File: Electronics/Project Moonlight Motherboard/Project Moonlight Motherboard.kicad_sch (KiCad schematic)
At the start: 42 parts, among them M1 AO3400A, M2 AO3400A, M3 AO3400A, U1 STM32F407IEHx, U2 TMC2209_SILENTSTEPSTICK, U3 TMC2209_SILENTSTEPSTICK, U4 TMC2209_SILENTSTEPSTICK, U5 TMC2209_SILENTSTEPSTICK

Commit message: whoops forgor to save it
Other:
- note added: "Auto Bed Leveling"
- note added: "Bed and Heater Mosfets"
- note added: "Fan Mosfets"
- note added: "I2C Display and Encoder"
- note added: "Power LED"
- note added: "Removable Stepper Drivers (XYZE)"
- note added: "Thermistors (T0, T1, T2)"
- moved on the sheet: ABL1, BED1, C1, C2, C3, C4, C5, C6, C7, FAN1, FAN2, FAN3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

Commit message: added a fuse
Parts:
- added F1: Fuse_Small, symbol Device:Fuse_Small
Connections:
- net VCC: now also F1.2; no longer PWR_IN.02
- new net: F1.1, PWR_IN.02
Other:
- moved on the sheet: PWR_IN

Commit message: fixed schematic & added 3d model for MCU
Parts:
- removed PWR_IN: 1751248, Phoenix 1751248:PHOENIX_1751248, symbol 1751248:1751248
- renumbered Z_END to Z_END1
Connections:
- net VCC: no longer PWR1.1
- net at F1.1: now also PWR1.1
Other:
- note added: "Power Jack"
- note removed: "Power LED"
- moved on the sheet: PWR1

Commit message: slowly updating lmao
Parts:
- added U6: STM32H563VITx, Package_QFP:LQFP-100_14x14mm_P0.5mm, symbol MCU_ST_STM32H5:STM32H563VITx
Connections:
- net +3V3: now also U6.100 (VDD), U6.11 (VDD), U6.22 (VDDA), U6.28 (VDD), U6.50 (VDD), U6.6 (VBAT), U6.73 (VDDUSB), U6.75 (VDD); no longer U1.C1 (VBAT), U1.C5 (VDD), U1.C7 (VDD), U1.C8 (VDD), U1.C9 (VDD), U1.F3 (VDD), U1.G13 (VDD), U1.G3 (VDD), U1.H13 (VDD), U1.J12 (VDD), U1.J13 (VDD), U1.K4 (VDD), U1.N10 (VDD), U1.N8 (VDD), U1.N9 (VDD), U1.R1 (VDDA)
- net ABL: now also U6.69 (PA10); no longer U1.D15 (PA10)
- net BED: now also U6.30 (PA5); no longer U1.P4 (PA5)
- net DIAG_M1: now also U6.18 (PC3); no longer U1.A10 (PB3)
- net DIAG_M2: now also U6.64 (PC7); no longer U1.B5 (PB7)
- net DIAG_M3: now also U6.79 (PC11); no longer U1.R13 (PB11)
- net DIAG_M4: now also U6.9 (PC15); no longer U1.R15 (PB15)
- net DIR_M1: now also U6.17 (PC2); no longer U1.M6 (PB2)
- net DIR_M2: now also U6.63 (PC6); no longer U1.B6 (PB6)
- net DIR_M3: now also U6.78 (PC10); no longer U1.R12 (PB10)
- net DIR_M4: now also U6.8 (PC14); no longer U1.R14 (PB14)
- net EN_BTN: now also U6.85 (PD4); no longer U1.J3 (PF4)
- net EN_FOR: now also U6.83 (PD2); no longer U1.H2 (PF2)
- net EN_M1: now also U6.15 (PC0); no longer U1.R5 (PB0)
- net EN_M2: now also U6.33 (PC4); no longer U1.A9 (PB4)
- net EN_M3: now also U6.65 (PC8); no longer U1.A5 (PB8)
- net EN_M4: now also U6.80 (PC12); no longer U1.P12 (PB12)
- net EN_REV: now also U6.84 (PD3); no longer U1.J2 (PF3)
- net FAN1: now also U6.31 (PA6); no longer U1.P3 (PA6)
- net FAN2: now also U6.32 (PA7); no longer U1.R3 (PA7)
- net FAN3: now also U6.67 (PA8); no longer U1.F15 (PA8)
- net GNDREF: now also U6.10 (VSS), U6.19 (VSSA), U6.27 (VSS), U6.49 (VSS), U6.74 (VSS), U6.99 (VSS); no longer U1.D5 (VSS), U1.D7 (VSS), U1.D8 (VSS), U1.D9 (VSS), U1.F10 (VSS), U1.F12 (VSS), U1.F2 (VSS), U1.F6 (VSS), U1.F7 (VSS), U1.F8 (VSS), U1.F9 (VSS), U1.G10 (VSS), U1.G12 (VSS), U1.G2 (VSS), U1.G6 (VSS), U1.G7 (VSS), U1.G8 (VSS), U1.G9 (VSS), U1.H10 (VSS), U1.H12 (VSS), U1.H6 (VSS), U1.H7 (VSS), U1.H8 (VSS), U1.H9 (VSS), U1.J10 (VSS), U1.J6 (VSS), U1.J7 (VSS), U1.J8 (VSS), U1.J9 (VSS), U1.K10 (VSS), U1.K6 (VSS), U1.K7 (VSS), U1.K8 (VSS), U1.K9 (VSS), U1.M1 (VSSA), U1.M8 (VSS), U1.M9 (VSS)
- net HOTEND: now also U6.29 (PA4); no longer U1.N4 (PA4)
- net SCRN_SCL: now also U6.82 (PD1); no longer U1.H3 (PF1)
- net SCRN_SDA: now also U6.81 (PD0); no longer U1.E2 (PF0)
- net STEP_M1: now also U6.16 (PC1); no longer U1.R4 (PB1)
- net STEP_M2: now also U6.34 (PC5); no longer U1.A6 (PB5)
- net STEP_M3: now also U6.66 (PC9); no longer U1.B4 (PB9)
- net STEP_M4: now also U6.7 (PC13); no longer U1.P13 (PB13)
- net T0: now also U6.23 (PA0); no longer U1.N3 (PA0)
- net T1: now also U6.24 (PA1); no longer U1.N2 (PA1)
- net T2: now also U6.25 (PA2); no longer U1.P2 (PA2)
- net Z_END: now also U6.70 (PA11); no longer U1.C15 (PA11)
- new net: U1.D5 (VSS), U1.D7 (VSS), U1.D8 (VSS), U1.D9 (VSS), U1.F10 (VSS), U1.F12 (VSS), U1.F2 (VSS), U1.F6 (VSS), U1.F7 (VSS), U1.F8 (VSS), U1.F9 (VSS), U1.G10 (VSS), U1.G12 (VSS), U1.G2 (VSS), U1.G6 (VSS), U1.G7 (VSS), U1.G8 (VSS), U1.G9 (VSS), U1.H10 (VSS), U1.H12 (VSS), U1.H6 (VSS), U1.H7 (VSS), U1.H8 (VSS), U1.H9 (VSS), U1.J10 (VSS), U1.J6 (VSS), U1.J7 (VSS), U1.J8 (VSS), U1.J9 (VSS), U1.K10 (VSS), U1.K6 (VSS), U1.K7 (VSS), U1.K8 (VSS), U1.K9 (VSS), U1.M8 (VSS), U1.M9 (VSS)
- new net: U1.G13 (VDD), U1.H13 (VDD), U1.J12 (VDD), U1.J13 (VDD), U1.K4 (VDD), U1.N10 (VDD), U1.N8 (VDD), U1.N9 (VDD), U1.R1 (VDDA)

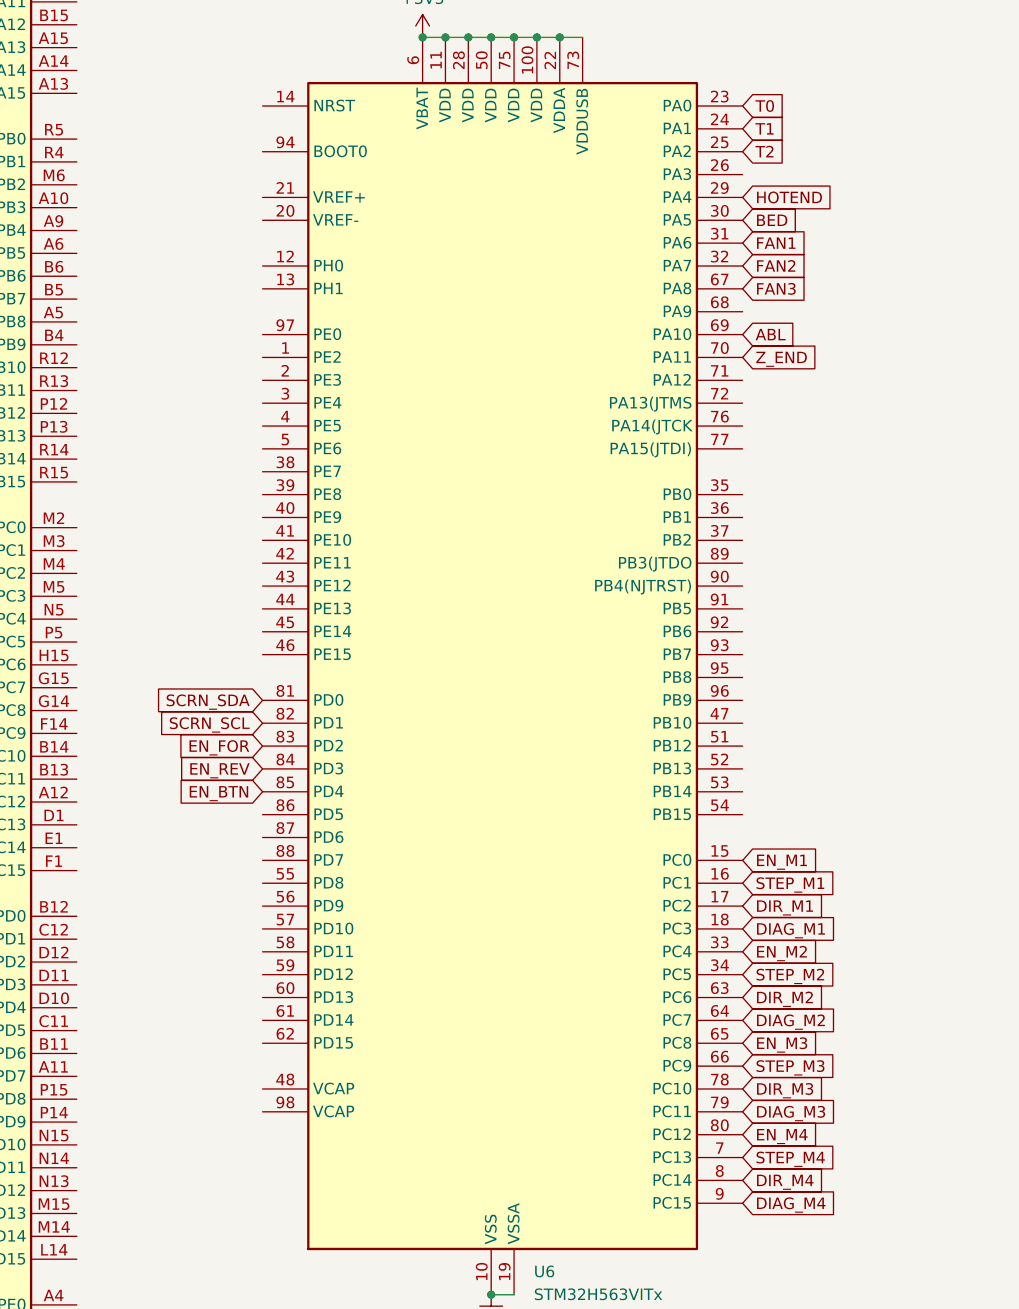
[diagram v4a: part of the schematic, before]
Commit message: added more parts and more routing done
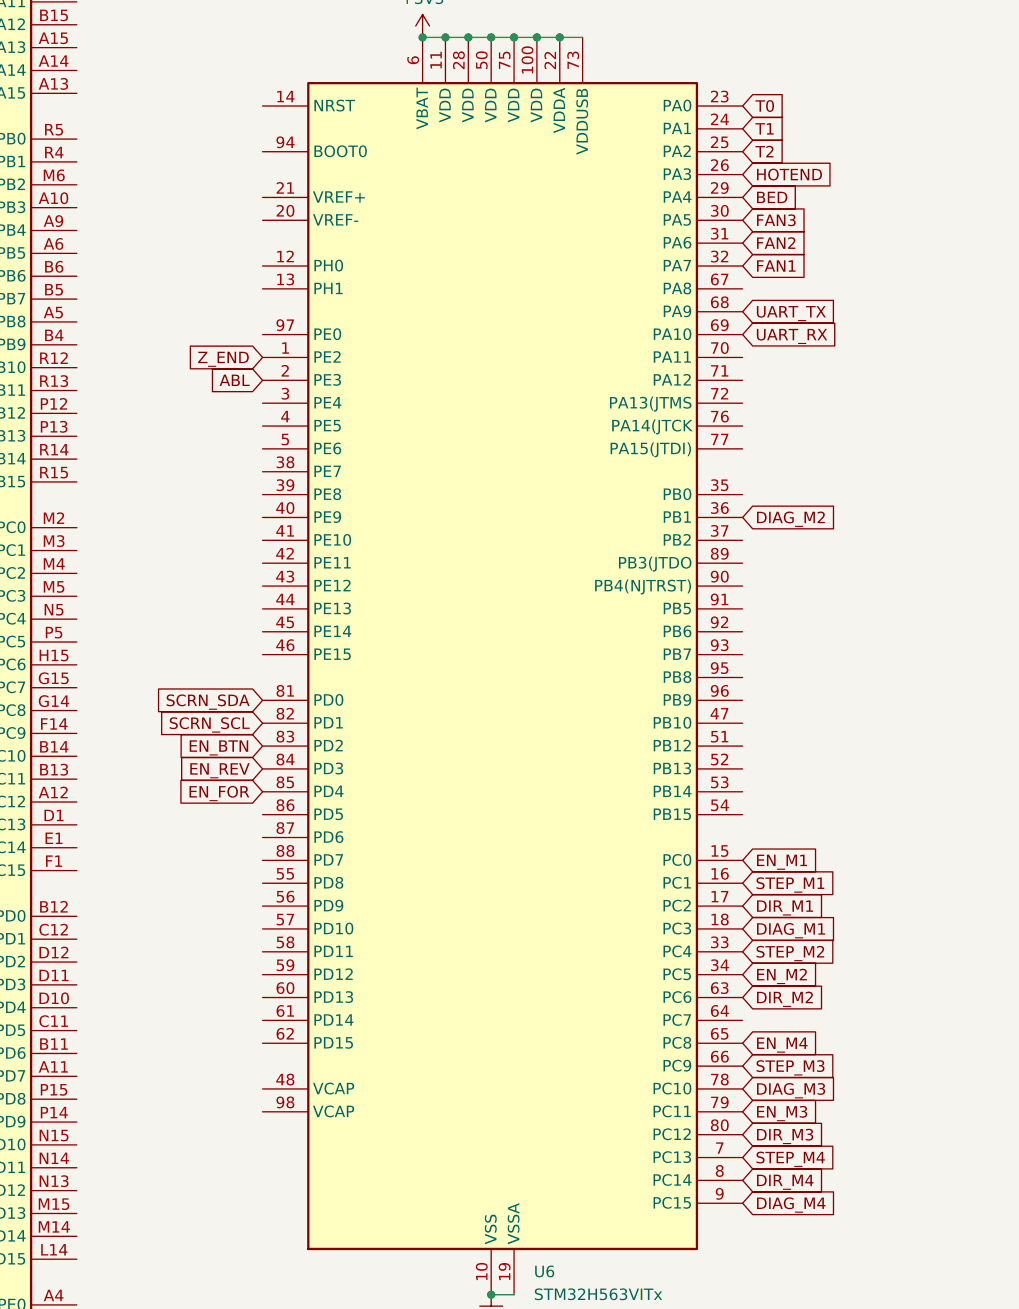
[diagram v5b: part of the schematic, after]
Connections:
- net ABL: now also U6.2 (PE3); no longer U6.69 (PA10)
- net BED: now also U6.29 (PA4); no longer U6.30 (PA5)
- net DIAG_M2: now also U6.36 (PB1); no longer U6.64 (PC7)
- net DIAG_M3: now also U6.78 (PC10); no longer U6.79 (PC11)
- net DIR_M3: now also U6.80 (PC12); no longer U6.78 (PC10)
- net EN_BTN: now also U6.83 (PD2); no longer U6.85 (PD4)
- net EN_FOR: now also U6.85 (PD4); no longer U6.83 (PD2)
- net EN_M2: now also U6.34 (PC5); no longer U6.33 (PC4)
- net EN_M3: now also U6.79 (PC11); no longer U6.65 (PC8)
- net EN_M4: now also U6.65 (PC8); no longer U6.80 (PC12)
- net FAN1: now also U6.32 (PA7); no longer U6.31 (PA6)
- net FAN2: now also U6.31 (PA6); no longer U6.32 (PA7)
- net FAN3: now also U6.30 (PA5); no longer U6.67 (PA8)
- net HOTEND: now also U6.26 (PA3); no longer U6.29 (PA4)
- net STEP_M2: now also U6.33 (PC4); no longer U6.34 (PC5)
- net UART_RX: now also U6.69 (PA10)
- net UART_TX: now also U6.68 (PA9)
- net Z_END: now also U6.1 (PE2); no longer U6.70 (PA11)

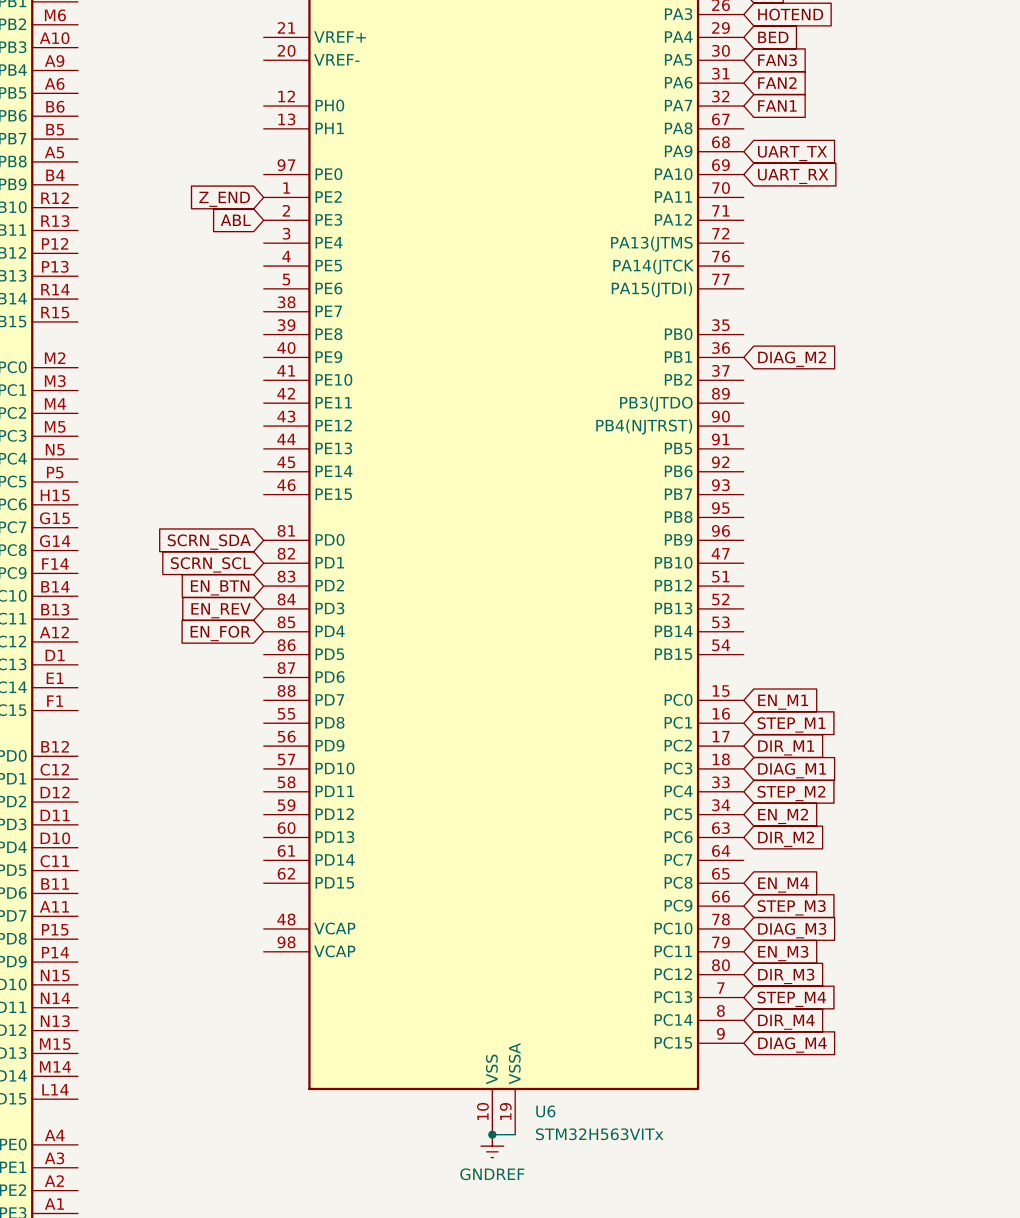
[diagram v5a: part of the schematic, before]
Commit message: added capacitors and routed a bunch of things
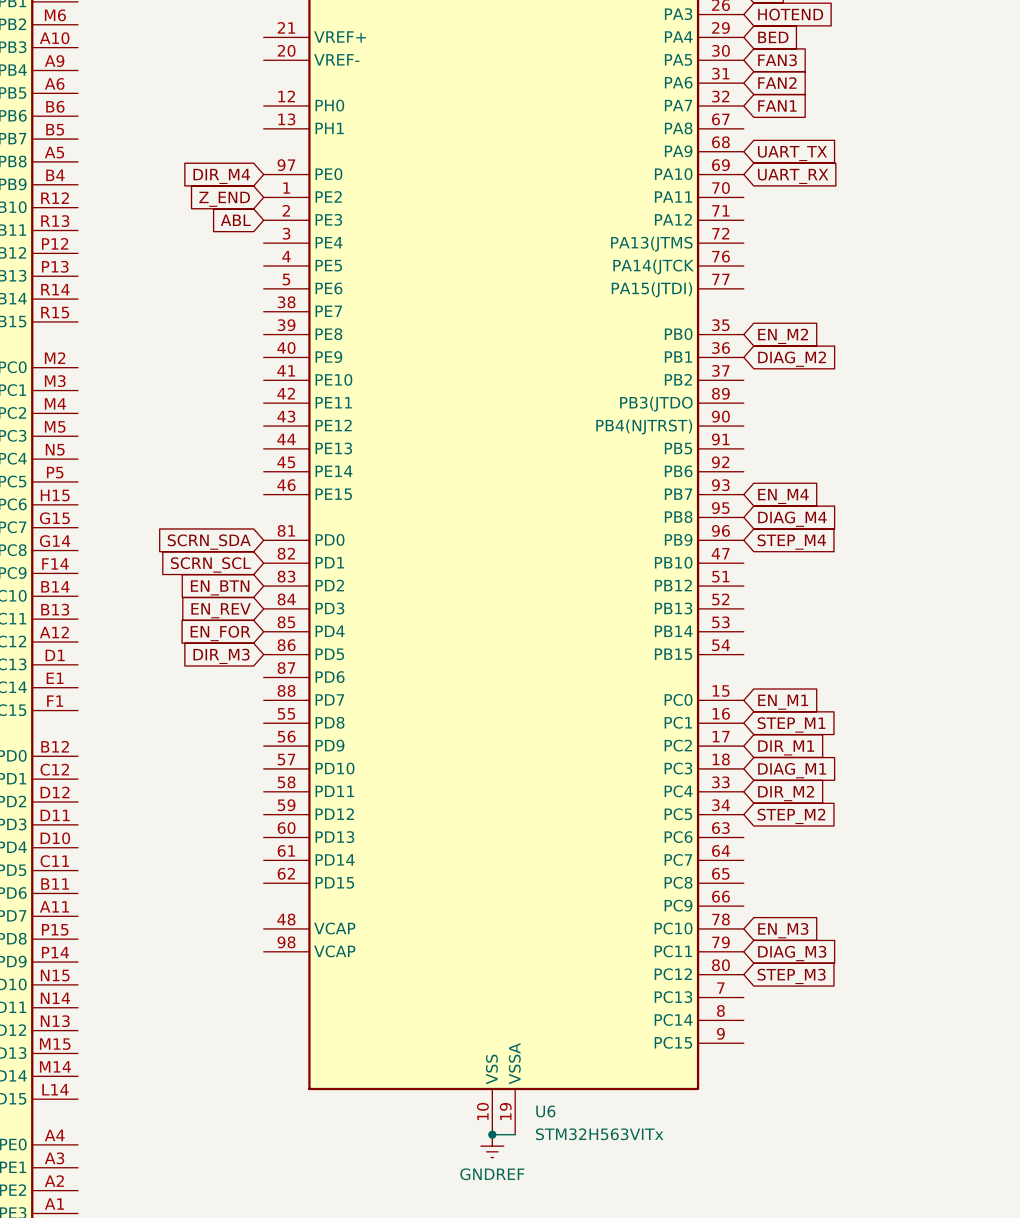
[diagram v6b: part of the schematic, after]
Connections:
- net DIAG_M3: now also U6.79 (PC11); no longer U6.78 (PC10)
- net DIAG_M4: now also U6.95 (PB8); no longer U6.9 (PC15)
- net DIR_M2: now also U6.33 (PC4); no longer U6.63 (PC6)
- net DIR_M3: now also U6.86 (PD5); no longer U6.80 (PC12)
- net DIR_M4: now also U6.97 (PE0); no longer U6.8 (PC14)
- net EN_M2: now also U6.35 (PB0); no longer U6.34 (PC5)
- net EN_M3: now also U6.78 (PC10); no longer U6.79 (PC11)
- net EN_M4: now also U6.93 (PB7); no longer U6.65 (PC8)
- net STEP_M2: now also U6.34 (PC5); no longer U6.33 (PC4)
- net STEP_M3: now also U6.80 (PC12); no longer U6.66 (PC9)
- net STEP_M4: now also U6.96 (PB9); no longer U6.7 (PC13)

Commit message: added debug header and programming USB port, tidied up silkscreen
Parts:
- removed U1: STM32F407IEHx, Package_BGA:UFBGA-201_10x10mm_Layout15x15_P0.65mm, symbol MCU_ST_STM32F4:STM32F407IEHx
- added DEBUG1: Conn_01x04_Pin, Connector_PinHeader_2.54mm:PinHeader_1x04_P2.54mm_Vertical, symbol Connector:Conn_01x04_Pin
- added USB1: 10118193-0001LF, 10118193-0001LF:AMPHENOL_10118193-0001LF, symbol 10118193-0001LF:10118193-0001LF
- C1, C2, C3, C4: footprint CAP_A750MV477M1VAAE018_KEM -> footprints:CAP_A750MV477M1VAAE018_KEM
- renumbered U6 to MCU1
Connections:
- net +3V3: now also DEBUG1.4 (Pin_4)
- net GNDREF: now also DEBUG1.2 (Pin_2), USB1.5 (GND)
- net USB_DM: now reaches MCU1.70 (PA11)
- net USB_DM: now also USB1.2 (D-)
- net USB_DP: now reaches MCU1.71 (PA12)
- net USB_DP: now also USB1.3 (D+)
- net SWDIO: now reaches MCU1.72 (PA13(JTMS)
- net SWDIO: now also DEBUG1.1 (Pin_1)
- net SWCLK: now reaches MCU1.76 (PA14(JTCK)
- net SWCLK: now also DEBUG1.3 (Pin_3)
- new net: USB1.S1 (SHIELD), USB1.S2 (SHIELD), USB1.S3 (SHIELD), USB1.S4 (SHIELD), USB1.S5 (SHIELD), USB1.S6 (SHIELD)
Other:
- note added: "Debug Interface"
- moved on the sheet: MCU1
